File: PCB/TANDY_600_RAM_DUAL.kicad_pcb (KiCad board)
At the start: 2 copper layers, 55.9 x 17.8 mm, 6 parts, among them J1 TANDY_600_RAM_DUAL, U1 628512, U2 74HC148, U3 74LVC1G02

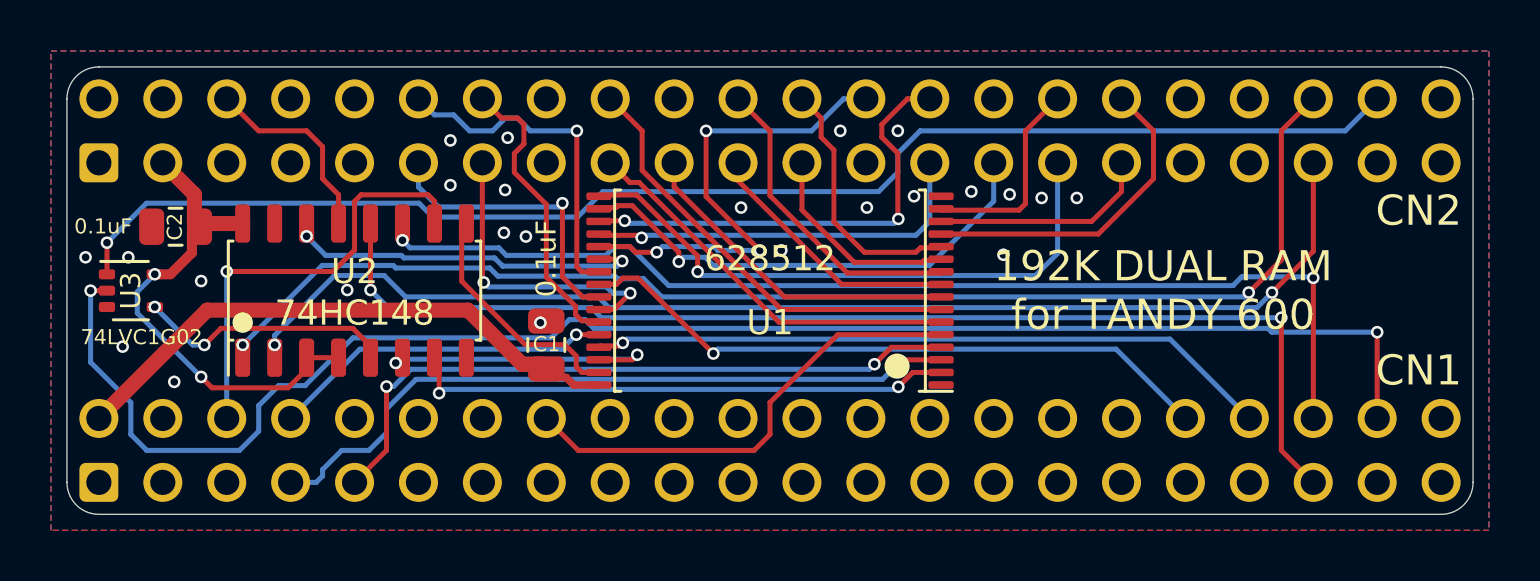
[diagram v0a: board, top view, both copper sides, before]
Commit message: wrong sram pinout on dual version
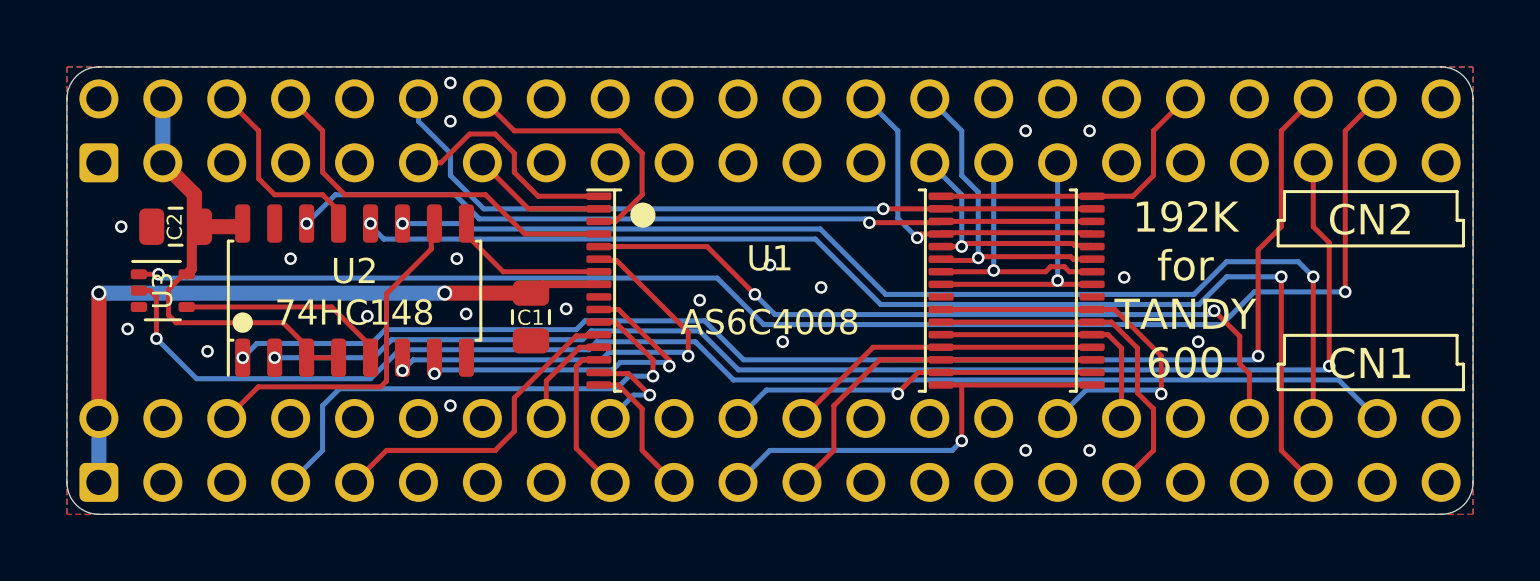
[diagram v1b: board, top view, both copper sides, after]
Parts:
- U1: value 628512 -> AS6C4008; footprint 000_LOCAL:TSOP32-14mm -> 000_LOCAL:TSOP32-dual
- moved U1 3.00 mm to (154.1, 109.2), turned to 0 degrees
- moved U3 1.27 mm to (127.0, 109.2)
- moved C1 1.27 mm to (141.6, 110.3), turned to -90 degrees
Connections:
- net /CS1A renamed /~{CS1A}
- net /CS1B renamed /~{CS1B}
- net /CS1C renamed /~{CS1C}
- net /CS1D renamed /~{CS1D}
- net /CS1E renamed /~{CS1E}
- net /CS1F renamed /~{CS1F}
- net Net-(U2-Pad5) renamed /CS2
- J1 pad CN1A1: (no net) -> VMEM
- J1 pad CN1A10: (no net) -> /A4
- J1 pad CN1A11: (no net) -> /A3
- J1 pad CN1A12: (no net) -> /A1
- J1 pad CN1A17: (no net) -> /D1
- J1 pad CN1A9: (no net) -> /A6
- J1 pad CN1B11: (no net) -> /A2
- J1 pad CN1B12: (no net) -> /A0
- J1 pad CN1B16: (no net) -> /D2
- J1 pad CN1B17: (no net) -> /D0
- J1 pad CN1B18: /~{OE} -> (no net)
- J1 pad CN1B4: /A13 -> (no net)
- J1 pad CN1B9: (no net) -> /A5
- J1 pad CN2A10: /A4 -> (no net)
- J1 pad CN2A11: /A3 -> (no net)
- J1 pad CN2A12: /A1 -> (no net)
- J1 pad CN2A17: /D1 -> (no net)
- J1 pad CN2A9: /A6 -> (no net)
- J1 pad CN2B11: /A2 -> (no net)
- J1 pad CN2B12: /A0 -> (no net)
- J1 pad CN2B16: /D2 -> (no net)
- J1 pad CN2B17: /D0 -> (no net)
- J1 pad CN2B18: (no net) -> /~{OE}
- J1 pad CN2B2: (no net) -> VCC
- J1 pad CN2B4: (no net) -> /A13
- J1 pad CN2B9: /A5 -> (no net)
- U1 pad 1: GND -> /A11
- U1 pad 10: /A2 -> /A16
- U1 pad 11: /A1 -> /A14
- U1 pad 12: /A0 -> /A12
- U1 pad 13: /D0 -> /A7
- U1 pad 14: /D1 -> /A6
- U1 pad 15: /D2 -> /A5
- U1 pad 16: GND -> /A4
- U1 pad 17: /D3 -> /A3
- U1 pad 18: /D4 -> /A2
- U1 pad 19: /D5 -> /A1
- U1 pad 2: /A16 -> /A9
- U1 pad 20: /D6 -> /A0
- U1 pad 21: /D7 -> /D0
- U1 pad 22: /~{CE} -> /D1
- U1 pad 23: /A10 -> /D2
- U1 pad 24: /~{OE} -> GND
- U1 pad 25: /A11 -> /D3
- U1 pad 26: /A9 -> /D4
- U1 pad 27: /A8 -> /D5
- U1 pad 28: /A13 -> /D6
- U1 pad 29: /~{WE} -> /D7
- U1 pad 3: /A14 -> /A8
- U1 pad 30: /A17 -> /~{CE}
- U1 pad 31: /A15 -> /A10
- U1 pad 32: VMEM -> /~{OE}
- U1 pad 4: /A12 -> /A13
- U1 pad 5: /A7 -> /~{WE}
- U1 pad 6: /A6 -> /A17
- U1 pad 7: /A5 -> /A15
- U1 pad 8: /A4 -> VMEM
- U1 pad 9: /A3 -> GND
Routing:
- net /~{CE}: track 14.1 -> 32.2 mm
- net /A10: track 13.6 -> 29.6 mm
- net /A7: track 18.9 -> 4.14 mm
- net /A12: track 27.0 -> 12.9 mm, vias 2 -> 0
- net /~{OE}: track 25.9 -> 12.4 mm, vias 1 -> 0
- net /A5: track 17.5 -> 4.36 mm, vias 0 -> 1
- net /D3: track 23.9 -> 10.8 mm
- net /CS2_B1: track 63.2 -> 53.5 mm, vias 2 -> 1
- net /A6: track 15.8 -> 6.18 mm
- net /D4: track 19.7 -> 10.5 mm
- net /A14: track 28.6 -> 20.6 mm
- net /A4: track 13.4 -> 5.56 mm
- net /A16: track 21.8 -> 14.1 mm
- net /D2: track 8.17 -> 15.7 mm, vias 0 -> 1
- net /A3: track 10.5 -> 17.8 mm, vias 0 -> 1
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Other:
- board text added: "${COMMENT2}"
- board text added: "${TITLE} v${REVISION}"
- board text added: "192K for TANDY 600"
- board text added: "C1,C2: ${6abd93ae-8309-4193-b5c6-e97f8e789dbe:VALUE} U3: ${89af72c0-2de0-4b8a-bd0f-646bca2cdb9a:VALUE}"
- board text removed: "${COMMENT2} v${REVISION}"
- board text removed: "192K DUAL RAM for TANDY 600"

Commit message: gnd on tiny, new dual sch, bus connector symbol & footprint
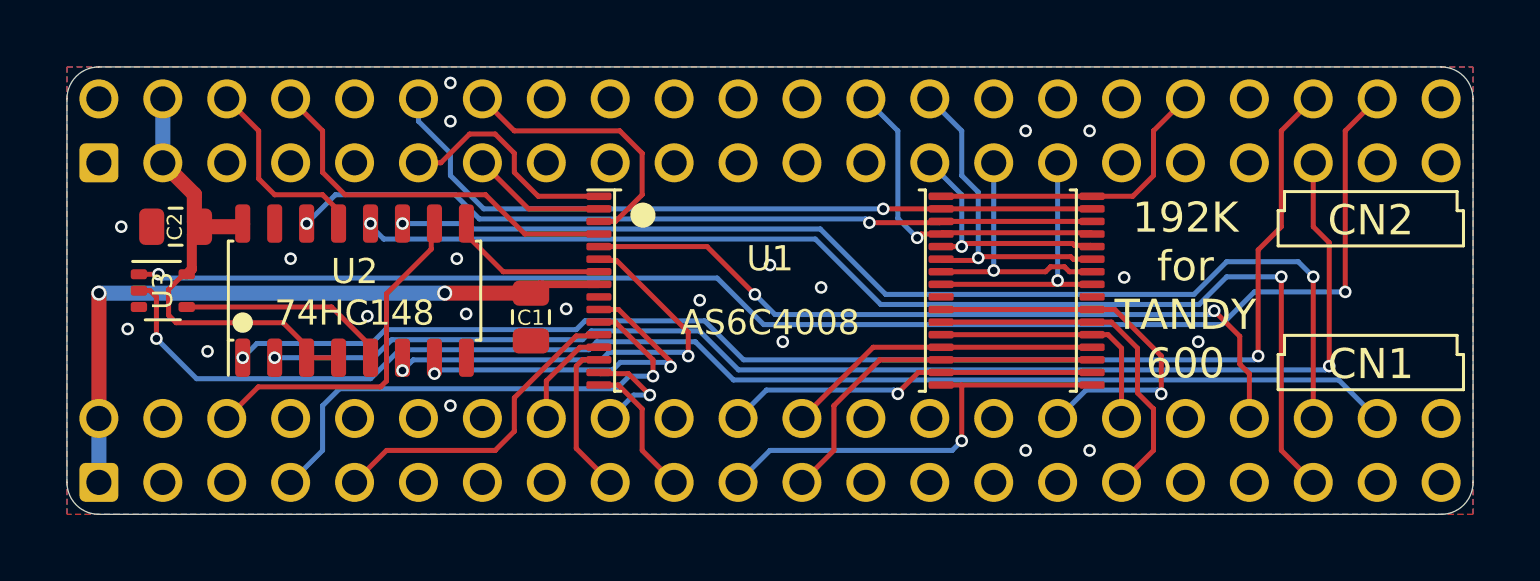
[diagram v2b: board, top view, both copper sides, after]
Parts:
- removed J1: TANDY_600_RAM_DUAL, 000_LOCAL:TANDY_600_RAM_DUAL
- added CN1: TANDY_600_RAM_BUS, 000_LOCAL:DIN41612-2x22_male_vertical, B.Cu at (151.1, 115.6)
- added CN2: TANDY_600_RAM_BUS, 000_LOCAL:DIN41612-2x22_male_vertical, B.Cu at (151.1, 102.9)
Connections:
- U2 pad 1: /~{CS1E} -> /~{B2_CS1_B}
- U2 pad 10: /~{CS1A} -> /~{B1_CS1_A}
- U2 pad 11: /~{CS1B} -> /~{B1_CS1_B}
- U2 pad 12: /~{CS1C} -> /~{B1_CS1_C}
- U2 pad 13: /~{CS1D} -> /~{B2_CS1_A}
- U2 pad 2: /~{CS1F} -> /~{B2_CS1_C}
- U3 pad 1: /CS2_B2 -> /B2_CS2
- U3 pad 2: /CS2_B1 -> /B1_CS2
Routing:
- net /CS2_B2: track 57.5 -> 0.00 mm, vias 2 -> 0
- net /B2_CS2: track 0.00 -> 57.5 mm, vias 0 -> 2
- net /CS2_B1: track 53.5 -> 0.00 mm, vias 1 -> 0
- net /B1_CS2: track 0.00 -> 53.5 mm, vias 0 -> 1
- net /~{CS1E}: track 52.8 -> 0.00 mm, vias 2 -> 0
- net /~{B2_CS1_B}: track 0.00 -> 52.8 mm, vias 0 -> 2
- net /~{CS1F}: track 51.4 -> 0.00 mm, vias 2 -> 0
- net /~{B2_CS1_C}: track 0.00 -> 51.4 mm, vias 0 -> 2
- net /~{CS1C}: track 46.7 -> 0.00 mm, vias 2 -> 0
- net /~{B1_CS1_C}: track 0.00 -> 46.7 mm, vias 0 -> 2
- net /~{CS1B}: track 43.8 -> 0.00 mm, vias 2 -> 0
- net /~{B1_CS1_B}: track 0.00 -> 43.8 mm, vias 0 -> 2
- net /~{CS1A}: track 14.0 -> 0.00 mm
- net /~{B1_CS1_A}: track 0.00 -> 14.0 mm
- net /~{CS1D}: track 7.91 -> 0.00 mm
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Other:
- board text added: "${COMMENT2} ${REVISION}"
- board text added: "this side down / pins this side"
- board text removed: "${COMMENT2}"
- board text removed: "${TITLE} v${REVISION}"

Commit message: add full-size dual
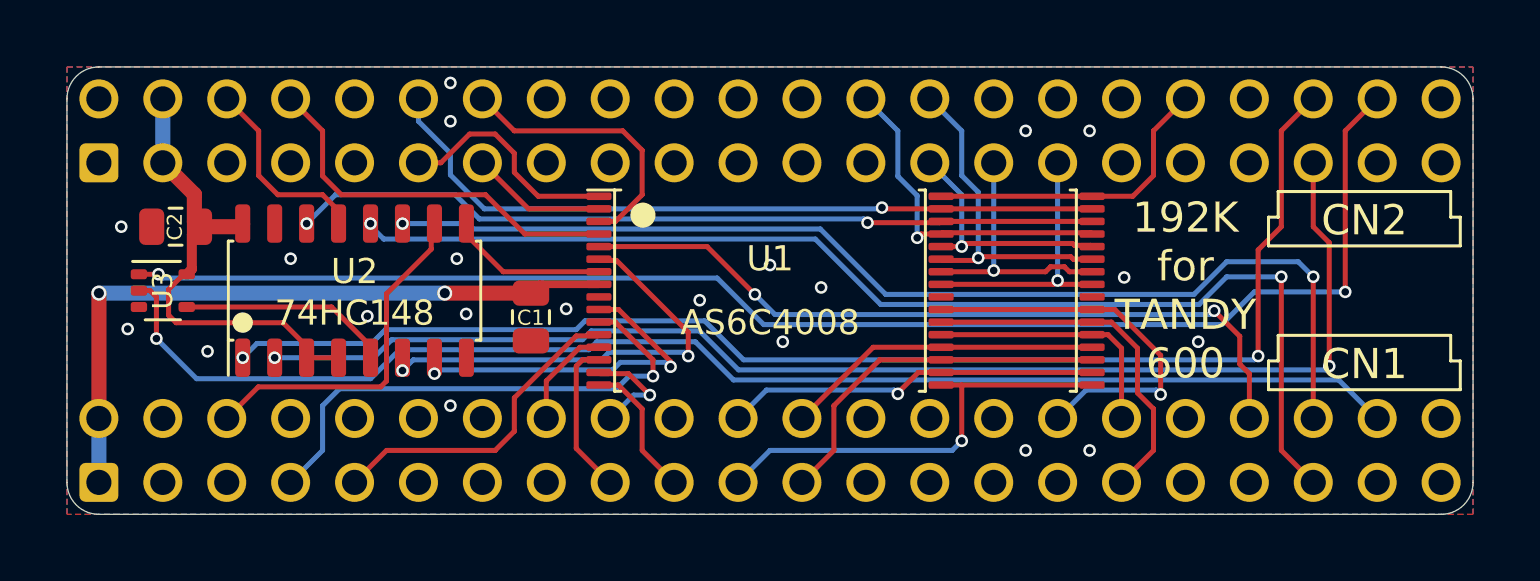
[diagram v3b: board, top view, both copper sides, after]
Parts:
- CN1, CN2: footprint 000_LOCAL:DIN41612-2x22_male_vertical -> 000_LOCAL:DIN41612-2x22_male_vertical_bare_pins

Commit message: footprints, ground paths
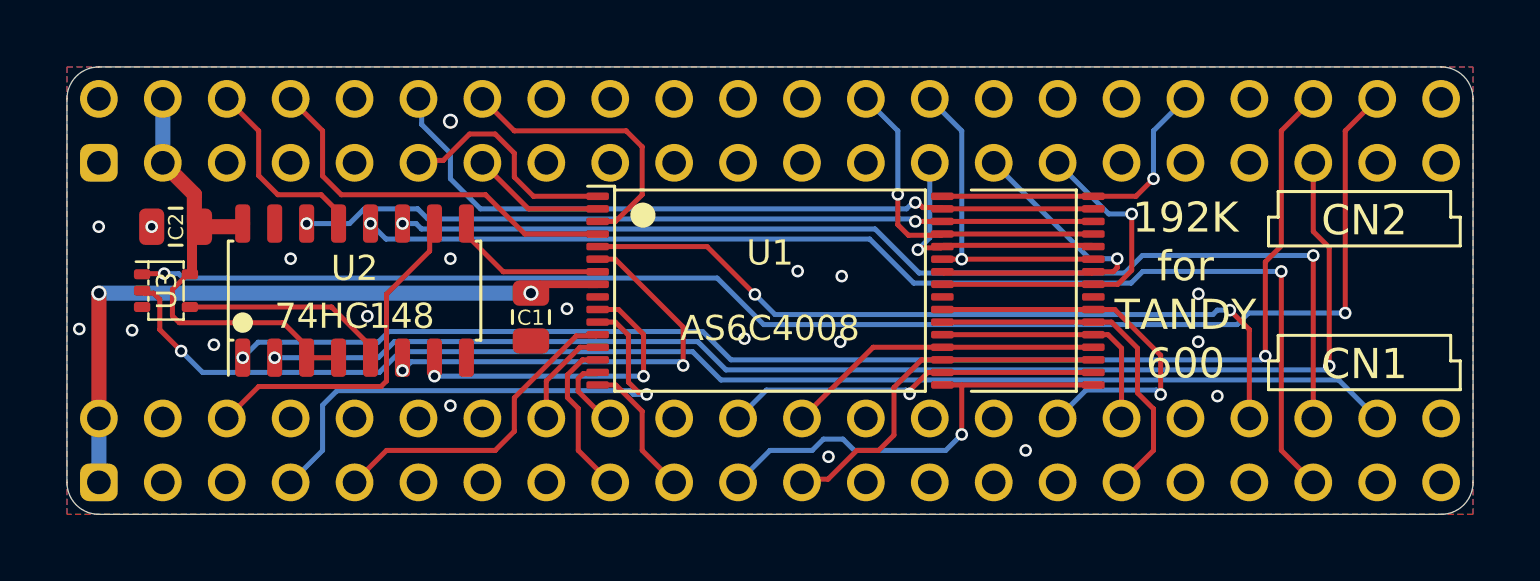
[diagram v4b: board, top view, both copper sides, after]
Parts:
- CN1, CN2: footprint 000_LOCAL:DIN41612-2x22_male_vertical_bare_pins -> 000_LOCAL:DIN-41612_02x22_male_vertical_bare_pins
- moved U3 0.13 mm to (127.1, 109.2)
- turned CN1 to 180 degrees
- turned CN2 to 180 degrees
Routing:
- net /D4: track 10.5 -> 13.9 mm
- net /D3: track 10.8 -> 13.8 mm
- net /A5: track 4.36 -> 3.10 mm, vias 1 -> 0
- net /A16: track 14.2 -> 12.9 mm
- net /B1_CS2: track 53.5 -> 52.6 mm
- net /D6: track 9.96 -> 10.7 mm
- net /~{OE}: vias 0 -> 1
- net GND: vias 21 -> 20

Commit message: dual_008
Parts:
- moved C1 2.00 mm to (141.7, 108.3), turned to 90 degrees
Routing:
- net /A14: track 21.0 -> 15.5 mm, vias 1 -> 0
- net /A16: track 12.9 -> 7.88 mm, vias 2 -> 0
- net /A17: track 17.9 -> 14.3 mm
- net /~{B1_CS1_B}: track 43.8 -> 42.4 mm
- net /~{B2_CS1_C}: track 51.0 -> 49.8 mm
- net /B2_CS2: track 57.9 -> 56.9 mm
- net /~{B1_CS1_C}: track 46.3 -> 45.7 mm
- net /~{WE}: track 30.9 -> 31.5 mm
- net /B1_CS2: track 52.6 -> 52.0 mm
- net /~{CE}: track 31.7 -> 32.2 mm
- net GND: vias 20 -> 15

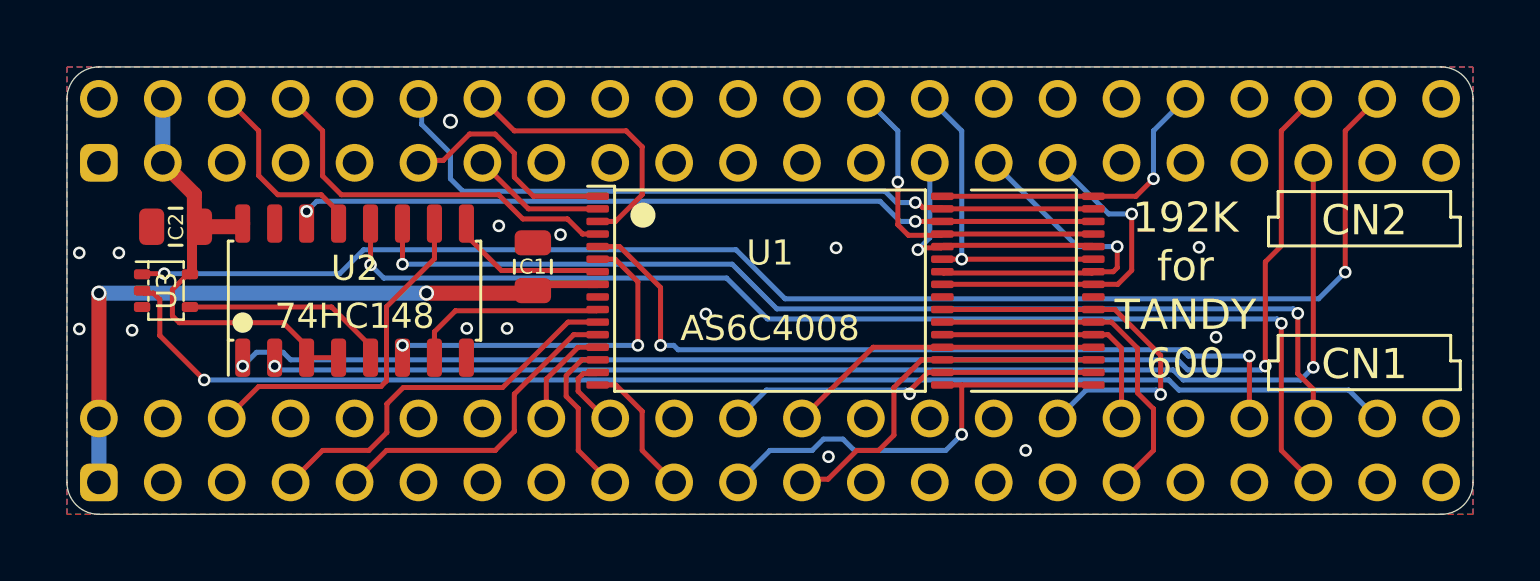
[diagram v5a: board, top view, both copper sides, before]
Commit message: support 256Kx8 chip on dual
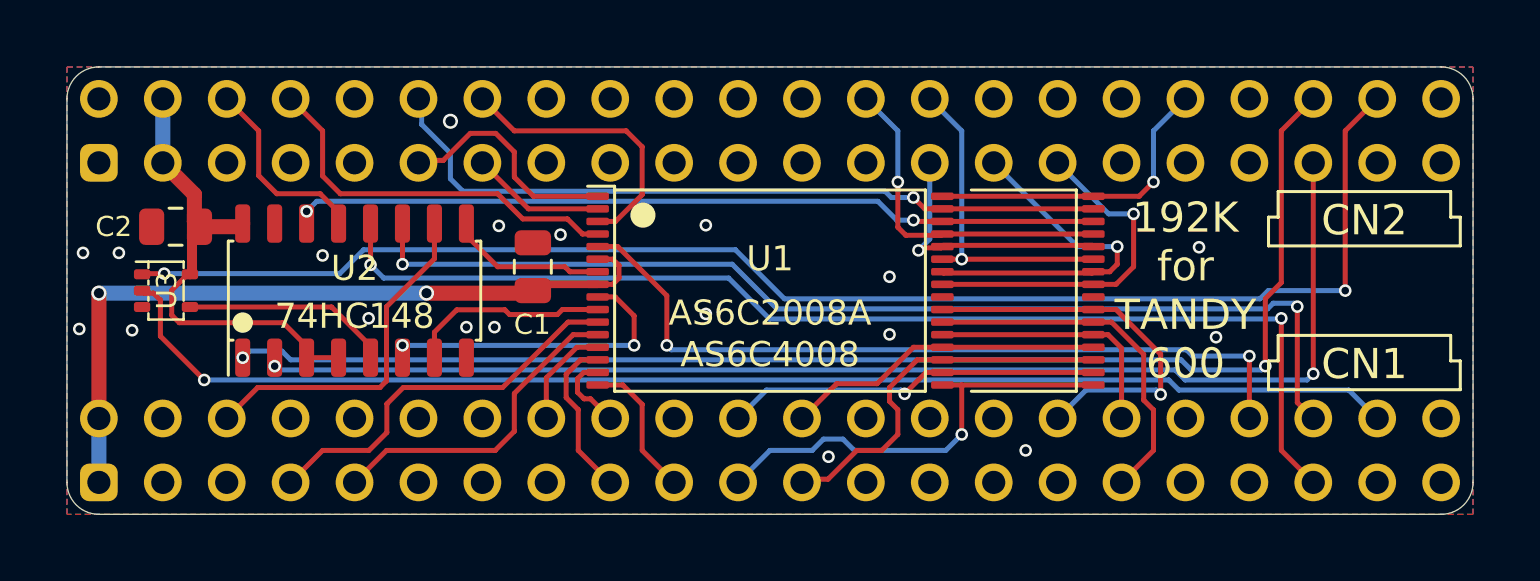
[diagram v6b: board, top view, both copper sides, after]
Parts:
- U1: value AS6C4008 -> AS6C2008A
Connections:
- U1 pad 6: /A17 -> VMEM
- U1 pad 9: GND -> /A17
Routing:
- net VMEM: track 27.5 -> 29.9 mm
- net /A17: track 14.3 -> 12.6 mm
- net GND: vias 15 -> 19

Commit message: dual version add /CE pullup for battery life
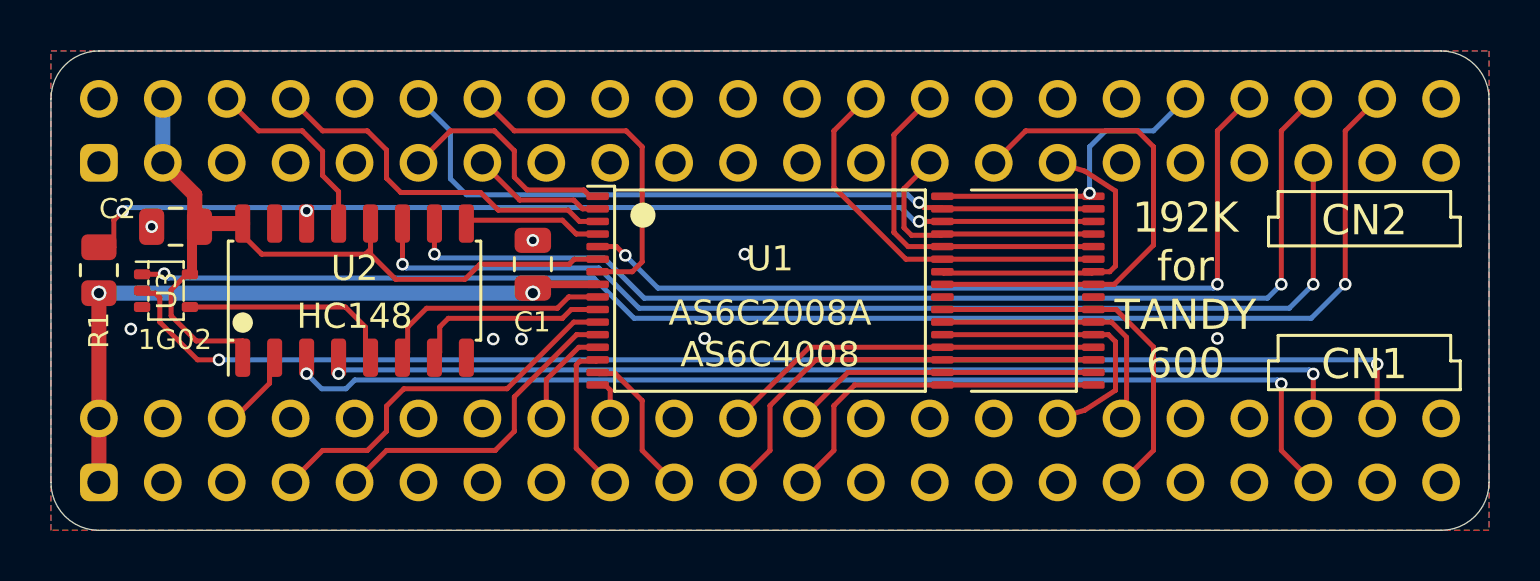
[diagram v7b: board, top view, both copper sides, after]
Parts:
- added R1: 200k, 000_LOCAL:R_0805, F.Cu at (124.5, 108.4)
- C1, C2: value 0.1uF -> 0.1u
- CN1, CN2: value TANDY_600_RAM_BUS -> TANDY_600_RAM_BUS_plain_pins
- U2: value 74HC148 -> HC148
- U3: value 74LVC1G02 -> 1G02
- moved C1 0.10 mm to (141.7, 108.2)
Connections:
- net /CS2 renamed /~{BUS_CS2}
- CN1 pad b19: /~{WE} -> unconnected-(CN1-~{WE}-Padb19)
- CN2 pad b19: unconnected-(CN2-Padb19) -> /~{WE}
- U1 pad 15: /A5 -> /A4
- U1 pad 16: /A4 -> /A5
- U1 pad 17: /A3 -> /A1
- U1 pad 18: /A2 -> /A0
- U1 pad 19: /A1 -> /A3
- U1 pad 20: /A0 -> /A2
- U1 pad 21: /D0 -> /D2
- U1 pad 22: /D1 -> /D0
- U1 pad 23: /D2 -> /D1
- U1 pad 25: /D3 -> /D4
- U1 pad 26: /D4 -> /D3
- U1 pad 27: /D5 -> /D7
- U1 pad 28: /D6 -> /D5
- U1 pad 29: /D7 -> /D6
- U1 pad 3: /A8 -> /A13
- U1 pad 4: /A13 -> /A15
- U1 pad 6: VMEM -> VCC
- U1 pad 7: /A15 -> /A8
- U2 pad 1: /~{B2_CS1_B} -> VCC
- U2 pad 10: /~{B1_CS1_A} -> /~{B2_CS1_B}
- U2 pad 11: /~{B1_CS1_B} -> /~{B2_CS1_C}
- U2 pad 12: /~{B1_CS1_C} -> VCC
- U2 pad 2: /~{B2_CS1_C} -> /~{B1_CS1_A}
- U2 pad 3: VCC -> /~{B1_CS1_C}
- U2 pad 4: VCC -> /~{B1_CS1_B}
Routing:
- net VCC: track 19.1 -> 32.6 mm
- net /~{B1_CS1_A}: track 14.0 -> 3.38 mm
- net /~{CE}: track 32.2 -> 41.6 mm, vias 2 -> 3
- net /~{B2_CS1_B}: track 52.5 -> 43.7 mm
- net /~{B2_CS1_C}: track 50.0 -> 43.8 mm
- net /D4: track 14.1 -> 20.1 mm, vias 1 -> 0
- net /D2: track 15.6 -> 11.5 mm, vias 1 -> 0
- net /A17: track 12.6 -> 9.35 mm, vias 2 -> 0
- net VMEM: track 29.9 -> 27.4 mm
- net /A8: track 11.3 -> 13.6 mm
- net /D7: track 13.5 -> 15.5 mm, vias 1 -> 0
- net /~{WE}: track 31.3 -> 33.3 mm
- net /~{B1_CS1_C}: track 45.8 -> 44.3 mm
- net /~{B1_CS1_B}: track 42.8 -> 41.3 mm
- net /A5: track 3.17 -> 1.71 mm
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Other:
- board size 55.9 x 17.8 mm -> 57.2 x 19.1 mm
- board text added: "C1,C2: ${6abd93ae-8309-4193-b5c6-e97f8e789dbe:VALUE} R1: ${0c359dbe-85cf-44c5-9fd0-3b040d8e3d19:VALUE}"
- board text removed: "C1,C2: ${6abd93ae-8309-4193-b5c6-e97f8e789dbe:VALUE} U3: ${89af72c0-2de0-4b8a-bd0f-646bca2cdb9a:VALUE}"
